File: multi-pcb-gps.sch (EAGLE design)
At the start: 8 parts, among them Q1 BS170, X1 6B-ZR

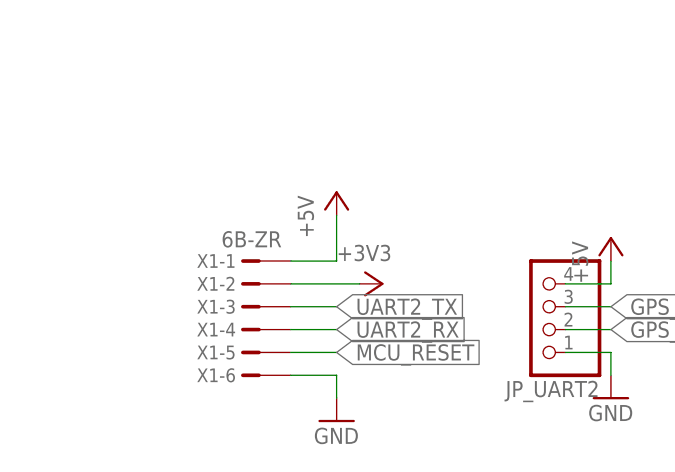
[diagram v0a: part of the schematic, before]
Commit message: Routed more multi-pcb boards
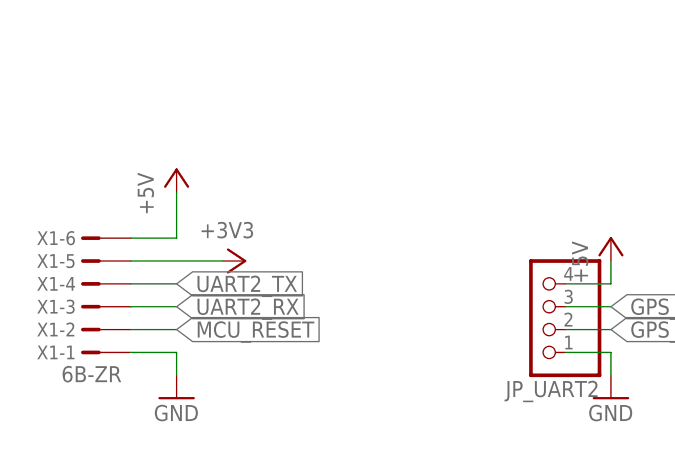
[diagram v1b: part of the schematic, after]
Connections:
- net +3V3: now also X1-5.1; no longer X1-2.1
- net +5V: now also X1-6.1; no longer X1-1.1
- net GND: now also X1-1.1; no longer X1-6.1
- net MCU_RESET: now also X1-2.1; no longer X1-5.1
- net UART2_RX: now also X1-3.1; no longer X1-4.1
- net UART2_TX: now also X1-4.1; no longer X1-3.1
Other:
- moved on the sheet: X1-1, X1-2, X1-3, X1-4, X1-5, X1-6
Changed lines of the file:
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@@
 <part name="R29" library="rcl" library_urn="urn:adsk.eagle:library:334" deviceset="R-EU_" device="0207/7" package3d_urn="urn:adsk.eagle:package:23493/2" value="10k"/>
 <part name="GND1" library="supply1" library_urn="urn:adsk.eagle:library:371" deviceset="GND" device=""/>
-<part name="X1" library="con-jst-custom" deviceset="?6B-ZR" device=""/>
 <part name="P+2" library="supply1" library_urn="urn:adsk.eagle:library:371" deviceset="+5V" device=""/>
 <part name="+3V1" library="supply1" library_urn="urn:adsk.eagle:library:371" deviceset="+3V3" device=""/>
+<part name="X1" library="con-jst-custom" deviceset="?6B-ZR" device=""/>
 </parts>
 <sheets>
@@
 <attribute name="VALUE" x="163.322" y="-24.13" size="1.778" layer="96" rot="R90"/>
 </instance>
-<instance part="GND1" gate="1" x="-170.18" y="-71.12" smashed="yes">
-<attribute name="VALUE" x="-172.72" y="-73.66" size="1.778" layer="96"/>
-</instance>
-<instance part="X1" gate="-1" x="-180.34" y="-53.34" smashed="yes" rot="MR0">
-<attribute name="NAME" x="-181.356" y="-54.102" size="1.524" layer="95" rot="MR0"/>
-<attribute name="VALUE" x="-176.276" y="-51.816" size="1.778" layer="96" rot="MR0"/>
-</instance>
-<instance part="X1" gate="-2" x="-180.34" y="-55.88" smashed="yes" rot="MR0">
-<attribute name="NAME" x="-181.356" y="-56.642" size="1.524" layer="95" rot="MR0"/>
-</instance>
-<instance part="X1" gate="-3" x="-180.34" y="-58.42" smashed="yes" rot="MR0">
-<attribute name="NAME" x="-181.356" y="-59.182" size="1.524" layer="95" rot="MR0"/>
-</instance>
-<instance part="X1" gate="-4" x="-180.34" y="-60.96" smashed="yes" rot="MR0">
-<attribute name="NAME" x="-181.356" y="-61.722" size="1.524" layer="95" rot="MR0"/>
-</instance>
-<instance part="X1" gate="-5" x="-180.34" y="-63.5" smashed="yes" rot="MR0">
-<attribute name="NAME" x="-181.356" y="-64.262" size="1.524" layer="95" rot="MR0"/>
-</instance>
-<instance part="X1" gate="-6" x="-180.34" y="-66.04" smashed="yes" rot="MR0">
-<attribute name="NAME" x="-181.356" y="-66.802" size="1.524" layer="95" rot="MR0"/>
-</instance>
-<instance part="P+2" gate="1" x="-170.18" y="-45.72" smashed="yes">
-<attribute name="VALUE" x="-172.72" y="-50.8" size="1.778" layer="96" rot="R90"/>
-</instance>
-<instance part="+3V1" gate="G$1" x="-165.1" y="-55.88" smashed="yes" rot="R270">
-<attribute name="VALUE" x="-170.18" y="-53.34" size="1.778" layer="96"/>
+<instance part="GND1" gate="1" x="-187.96" y="-68.58" smashed="yes">
+<attribute name="VALUE" x="-190.5" y="-71.12" size="1.778" layer="96"/>
+</instance>
+<instance part="P+2" gate="1" x="-187.96" y="-43.18" smashed="yes">
+<attribute name="VALUE" x="-190.5" y="-48.26" size="1.778" layer="96" rot="R90"/>
+</instance>
+<instance part="+3V1" gate="G$1" x="-180.34" y="-53.34" smashed="yes" rot="R270">
+<attribute name="VALUE" x="-185.42" y="-50.8" size="1.778" layer="96"/>
+</instance>
+<instance part="X1" gate="-1" x="-198.12" y="-63.5" smashed="yes" rot="R180">
+<attribute name="NAME" x="-199.136" y="-62.738" size="1.524" layer="95" rot="R180"/>
+<attribute name="VALUE" x="-194.056" y="-65.024" size="1.778" layer="96" rot="R180"/>
+</instance>
+<instance part="X1" gate="-2" x="-198.12" y="-60.96" smashed="yes" rot="R180">
+<attribute name="NAME" x="-199.136" y="-60.198" size="1.524" layer="95" rot="R180"/>
+</instance>
+<instance part="X1" gate="-3" x="-198.12" y="-58.42" smashed="yes" rot="R180">
+<attribute name="NAME" x="-199.136" y="-57.658" size="1.524" layer="95" rot="R180"/>
+</instance>
+<instance part="X1" gate="-4" x="-198.12" y="-55.88" smashed="yes" rot="R180">
+<attribute name="NAME" x="-199.136" y="-55.118" size="1.524" layer="95" rot="R180"/>
+</instance>
+<instance part="X1" gate="-5" x="-198.12" y="-53.34" smashed="yes" rot="R180">
+<attribute name="NAME" x="-199.136" y="-52.578" size="1.524" layer="95" rot="R180"/>
+</instance>
+<instance part="X1" gate="-6" x="-198.12" y="-50.8" smashed="yes" rot="R180">
+<attribute name="NAME" x="-199.136" y="-50.038" size="1.524" layer="95" rot="R180"/>
 </instance>
 </instances>
@@
 </segment>
 <segment>
-<pinref part="X1" gate="-2" pin="1"/>
+<pinref part="X1" gate="-5" pin="1"/>
 <pinref part="+3V1" gate="G$1" pin="+3V3"/>
-<wire x1="-175.26" y1="-55.88" x2="-167.64" y2="-55.88" width="0.1524" layer="91"/>
+<wire x1="-193.04" y1="-53.34" x2="-182.88" y2="-53.34" width="0.1524" layer="91"/>
 </segment>
 </net>
@@
 </segment>
 <segment>
-<wire x1="-175.26" y1="-66.04" x2="-170.18" y2="-66.04" width="0.1524" layer="91"/>
 <pinref part="GND1" gate="1" pin="GND"/>
-<wire x1="-170.18" y1="-66.04" x2="-170.18" y2="-68.58" width="0.1524" layer="91"/>
-<pinref part="X1" gate="-6" pin="1"/>
+<wire x1="-187.96" y1="-63.5" x2="-187.96" y2="-66.04" width="0.1524" layer="91"/>
+<pinref part="X1" gate="-1" pin="1"/>
+<wire x1="-193.04" y1="-63.5" x2="-187.96" y2="-63.5" width="0.1524" layer="91"/>
 </segment>
 </net>
@@
 <segment>
 <pinref part="P+2" gate="1" pin="+5V"/>
-<pinref part="X1" gate="-1" pin="1"/>
-<wire x1="-170.18" y1="-48.26" x2="-170.18" y2="-53.34" width="0.1524" layer="91"/>
-<wire x1="-170.18" y1="-53.34" x2="-175.26" y2="-53.34" width="0.1524" layer="91"/>
+<wire x1="-187.96" y1="-45.72" x2="-187.96" y2="-50.8" width="0.1524" layer="91"/>
+<pinref part="X1" gate="-6" pin="1"/>
+<wire x1="-193.04" y1="-50.8" x2="-187.96" y2="-50.8" width="0.1524" layer="91"/>
 </segment>
 </net>
@@
 </segment>
 <segment>
-<label x="-170.18" y="-60.96" size="1.778" layer="95" xref="yes"/>
-<wire x1="-170.18" y1="-60.96" x2="-175.26" y2="-60.96" width="0.1524" layer="91"/>
-<pinref part="X1" gate="-4" pin="1"/>
+<label x="-187.96" y="-58.42" size="1.778" layer="95" xref="yes"/>
+<pinref part="X1" gate="-3" pin="1"/>
+<wire x1="-193.04" y1="-58.42" x2="-187.96" y2="-58.42" width="0.1524" layer="91"/>
 </segment>
 </net>
@@
 </segment>
 <segment>
-<label x="-170.18" y="-58.42" size="1.778" layer="95" xref="yes"/>
-<wire x1="-175.26" y1="-58.42" x2="-170.18" y2="-58.42" width="0.1524" layer="91"/>
-<pinref part="X1" gate="-3" pin="1"/>
+<label x="-187.96" y="-55.88" size="1.778" layer="95" xref="yes"/>
+<pinref part="X1" gate="-4" pin="1"/>
+<wire x1="-193.04" y1="-55.88" x2="-187.96" y2="-55.88" width="0.1524" layer="91"/>
 </segment>
 </net>
@@
 </segment>
 <segment>
-<wire x1="-175.26" y1="-63.5" x2="-170.18" y2="-63.5" width="0.1524" layer="91"/>
-<label x="-170.18" y="-63.5" size="1.778" layer="95" xref="yes"/>
-<pinref part="X1" gate="-5" pin="1"/>
-</segment>
-</net>
+<label x="-187.96" y="-60.96" size="1.778" layer="95" xref="yes"/>
+<pinref part="X1" gate="-2" pin="1"/>
+<wire x1="-187.96" y1="-60.96" x2="-193.04" y2="-60.96" width="0.1524" layer="91"/>
+</segment>
+</net>

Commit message: Made schematic more compact/clean
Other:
- moved on the sheet: JP_UART2, Q1, R16, R22, R23, R29, X1-1, X1-2, X1-3, X1-4, X1-5, X1-6

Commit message: updated some PCB's
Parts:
- Q1: value BS170 -> BS170WIDE; device transistor-small-signal:BS170 -> samuel:BS170WIDE
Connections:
- net MCU_RESET: now also X1-4.1; no longer X1-2.1
- net UART2_TX: now also X1-2.1; no longer X1-4.1
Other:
- note added: "For debugging"
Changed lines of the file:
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@@
 <part name="+3V6" library="supply1" library_urn="urn:adsk.eagle:library:371" deviceset="+3V3" device=""/>
 <part name="R16" library="rcl" library_urn="urn:adsk.eagle:library:334" deviceset="R-EU_" device="0207/7" package3d_urn="urn:adsk.eagle:package:23493/2" value="5k"/>
-<part name="Q1" library="transistor-small-signal" library_urn="urn:adsk.eagle:library:401" deviceset="BS170" device="" package3d_urn="urn:adsk.eagle:package:29751/2"/>
+<part name="Q1" library="samuel" deviceset="BS170" device="WIDE"/>
 <part name="R22" library="rcl" library_urn="urn:adsk.eagle:library:334" deviceset="R-EU_" device="0207/7" package3d_urn="urn:adsk.eagle:package:23493/2" value="10k"/>
 <part name="R23" library="rcl" library_urn="urn:adsk.eagle:library:334" deviceset="R-EU_" device="0207/7" package3d_urn="urn:adsk.eagle:package:23493/2" value="10k"/>
@@
 <text x="66.04" y="86.36" size="1.778" layer="97">Checked</text>
 <text x="38.1" y="86.36" size="1.778" layer="97">LEVEL CONVERTER</text>
+<text x="-40.64" y="116.84" size="1.778" layer="97">For debugging</text>
 </plain>
 <instances>
@@
 </segment>
 <segment>
-<label x="-30.48" y="142.24" size="1.778" layer="95" xref="yes"/>
-<pinref part="X1" gate="-4" pin="1"/>
-<wire x1="-35.56" y1="142.24" x2="-30.48" y2="142.24" width="0.1524" layer="91"/>
+<label x="-30.48" y="137.16" size="1.778" layer="95" xref="yes"/>
+<pinref part="X1" gate="-2" pin="1"/>
+<wire x1="-30.48" y1="137.16" x2="-35.56" y2="137.16" width="0.1524" layer="91"/>
 </segment>
 </net>
@@
 </segment>
 <segment>
-<label x="-30.48" y="137.16" size="1.778" layer="95" xref="yes"/>
-<pinref part="X1" gate="-2" pin="1"/>
-<wire x1="-30.48" y1="137.16" x2="-35.56" y2="137.16" width="0.1524" layer="91"/>
-</segment>
-</net>
+<label x="-30.48" y="142.24" size="1.778" layer="95" xref="yes"/>
+<pinref part="X1" gate="-4" pin="1"/>
+<wire x1="-35.56" y1="142.24" x2="-30.48" y2="142.24" width="0.1524" layer="91"/>
+</segment>
+</net>
